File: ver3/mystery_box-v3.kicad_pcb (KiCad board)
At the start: 2 copper layers, 136 x 100 mm, 61 parts, among them J1 Screw_Terminal_01x02, J10 Screw_Terminal_01x02, J11 Screw_Terminal_01x02, J12 Screw_Terminal_01x02, J13 Screw_Terminal_01x02, J14 Screw_Terminal_01x02, J15 Screw_Terminal_01x02, J16 Screw_Terminal_01x02, J17 Screw_Terminal_01x02, J18 Barrel_Jack_MountingPin, J20 rj45-CC-X2-Aliexpress, J3 SERIAL1, J8 Screw_Terminal_01x02, J9 Screw_Terminal_01x02, Q1 IRLZ44N, Q2 IRLZ44N, Q3 IRLZ44N, SW01 Screw_Terminal_01x02, SW02 Screw_Terminal_01x02, SW03 Screw_Terminal_01x02, U1 THVD1400D

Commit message: ver3 rev 2.0 prep for at.\tension
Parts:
- removed R5: 1k, Resistor_THT:R_Axial_DIN0207_L6.3mm_D2.5mm_P10.16mm_Horizontal
- added D5: D_Zener, Diode_THT:D_A-405_P7.62mm_Horizontal, F.Cu at (250.5, 78.8)
- moved PWR_12V_FAN1 59.4 mm to (209.5, 42.0), turned to 180 degrees
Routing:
- net VCC 12V: track 202.5 -> 205.8 mm
- net VCC 12V SW: track 360.8 -> 361.7 mm
- net Net-(D5-A): track 4.97 -> 5.82 mm
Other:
- board text added: "12V"
- board text added: "12V fused"
- board text added: "5V"
- board text added: "DO NOT SET when USB is connected!"
- board text added: "ETH"
- board text added: "In+"
- board text added: "In-"
- board text added: "Must select unfused 12V source on JMP_BUCK_PWR1"
- board text added: "Out+"
- board text added: "Out-"
- board text added: "POE"
- board text added: "Select POE voltage unfused 12V or unfused 24V from boost converter"
- board text added: "Select whether 5V Buck converter is powered from fused or unfused 12V supply"
- board text added: "Set to supply controller from onboard 5V"
- board text added: "USB-C"
- board text added: "rev. 2.0"
- board text removed: "rev. 1.0"

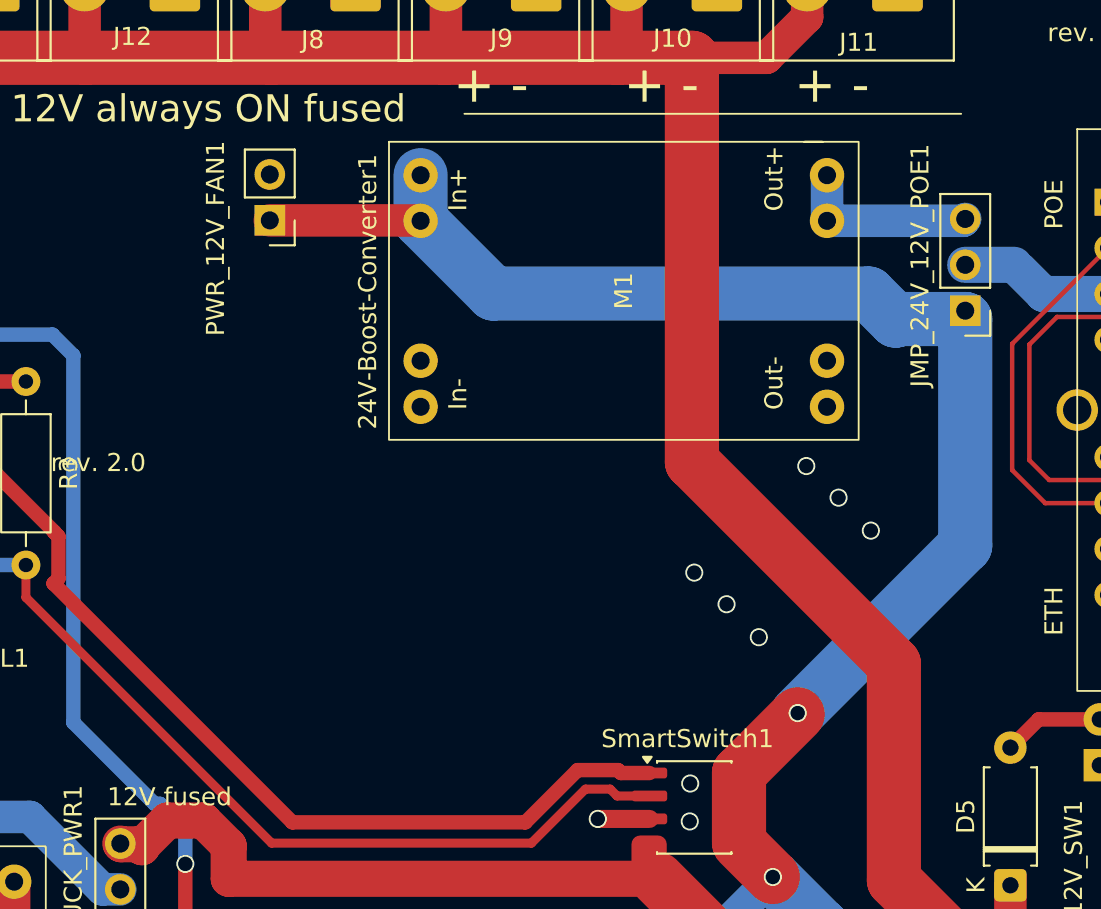
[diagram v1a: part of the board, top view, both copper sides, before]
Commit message: new 24v boost converter module
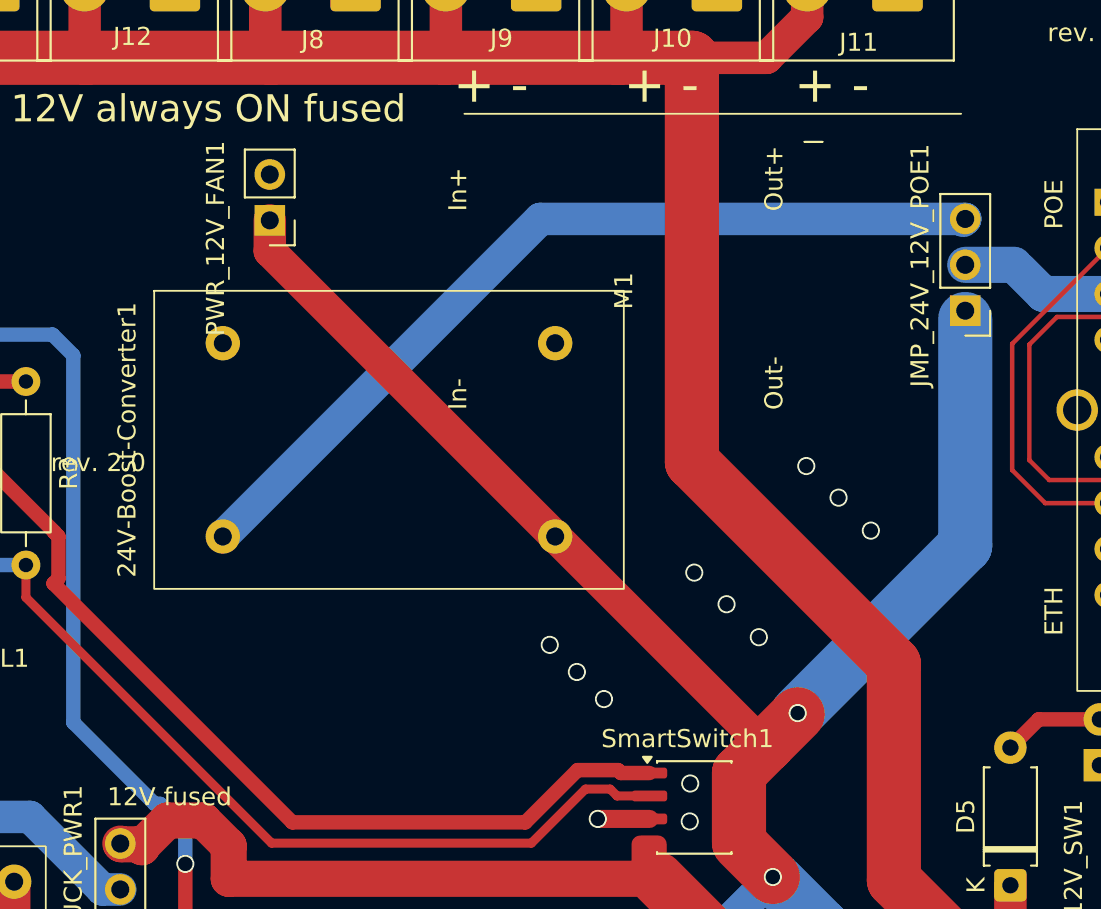
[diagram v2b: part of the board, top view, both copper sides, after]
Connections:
- 24V-Boost-Converter1 pad 2: VCC 12V -> GND
- 24V-Boost-Converter1 pad 3: GND -> VCC 24V
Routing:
- net VCC 24V: track 10.4 -> 48.5 mm
- net VCC 12V: track 205.8 -> 203.0 mm
- net GND: vias 27 -> 30
